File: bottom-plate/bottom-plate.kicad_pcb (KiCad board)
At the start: 2 copper layers, 274.1 x 106.7 mm, 19 parts

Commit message: added logos on silkscreen and plotted all gerber files again
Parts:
- removed the G*** at (158.6, 95.6)
- removed the G*** at (138.5, 95.8)
- removed REF** (x6): Breakaway_Tabs, kbd:Breakaway_Tabs
- removed the Ref** at (248.4, 79.5)
- removed the Ref** at (246.5, 37.4)
- removed the Ref** at (199.2, 80.1)
- removed the Ref** at (269.5, 69.3)
- removed the Ref** at (280.4, 78.5)
- removed the Ref** at (52.0, 85.5)
- removed the Ref** at (98.1, 80.4)
- removed the Ref** at (126.6, 40.9)
- removed the Ref** at (50.7, 37.5)
- removed the Ref** at (27.7, 69.3)
- removed the Ref** at (170.7, 40.9)
- added G***: LOGO, logo:jdkbd-logo1, F.Cu at (47.0, 45.8)
- added G***: LOGO, logo:jdkbd-logo1, B.Cu at (47.0, 45.8)
- added Ref**: Val**, kbd:M2_HOLE_v2, B.Cu at (38.4, 86.7)
- added Ref**: Val**, kbd:M2_HOLE_v2, B.Cu at (148.1, 49.1)
- added Ref**: Val**, kbd:M2_HOLE_v2, B.Cu at (72.2, 45.7)
- added Ref**: Val**, kbd:M2_HOLE_v2, B.Cu at (119.6, 88.4)
- added Ref**: Val**, kbd:M2_HOLE_v2, B.Cu at (70.4, 87.8)
- added Ref**: Val**, kbd:M2_HOLE_v2, B.Cu at (149.4, 86.4)
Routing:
- added copper zone on B.Cu, net (none)
- added copper zone on F.Cu, net (none)
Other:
- board size 274.1 x 106.7 mm -> 134.8 x 106.7 mm
- board text removed: "cornetrack pcb - designed by jannikwibker"
- board text removed: "left pcb"
- board text removed: "right pcb"

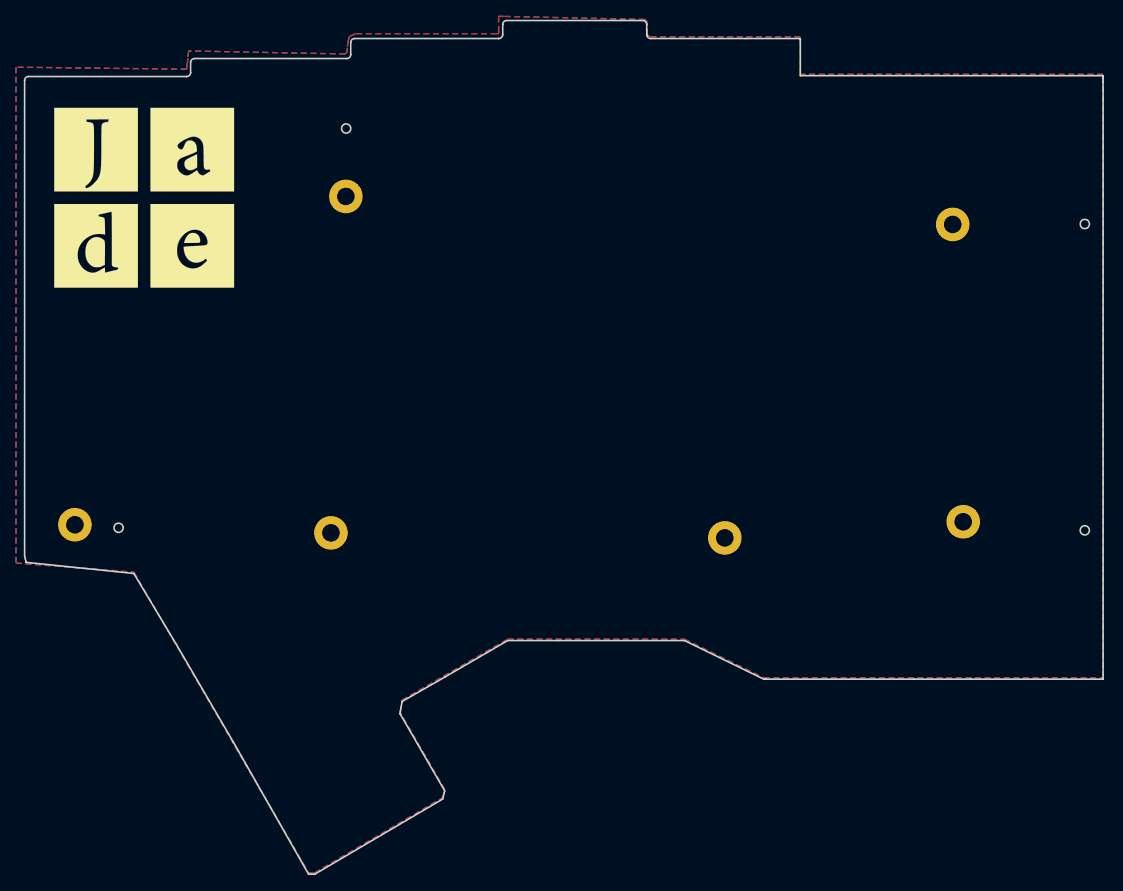
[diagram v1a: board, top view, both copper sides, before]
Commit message: made top and bottom plate a tiny bit larger in order to increase distance between edge cuts to >2mm
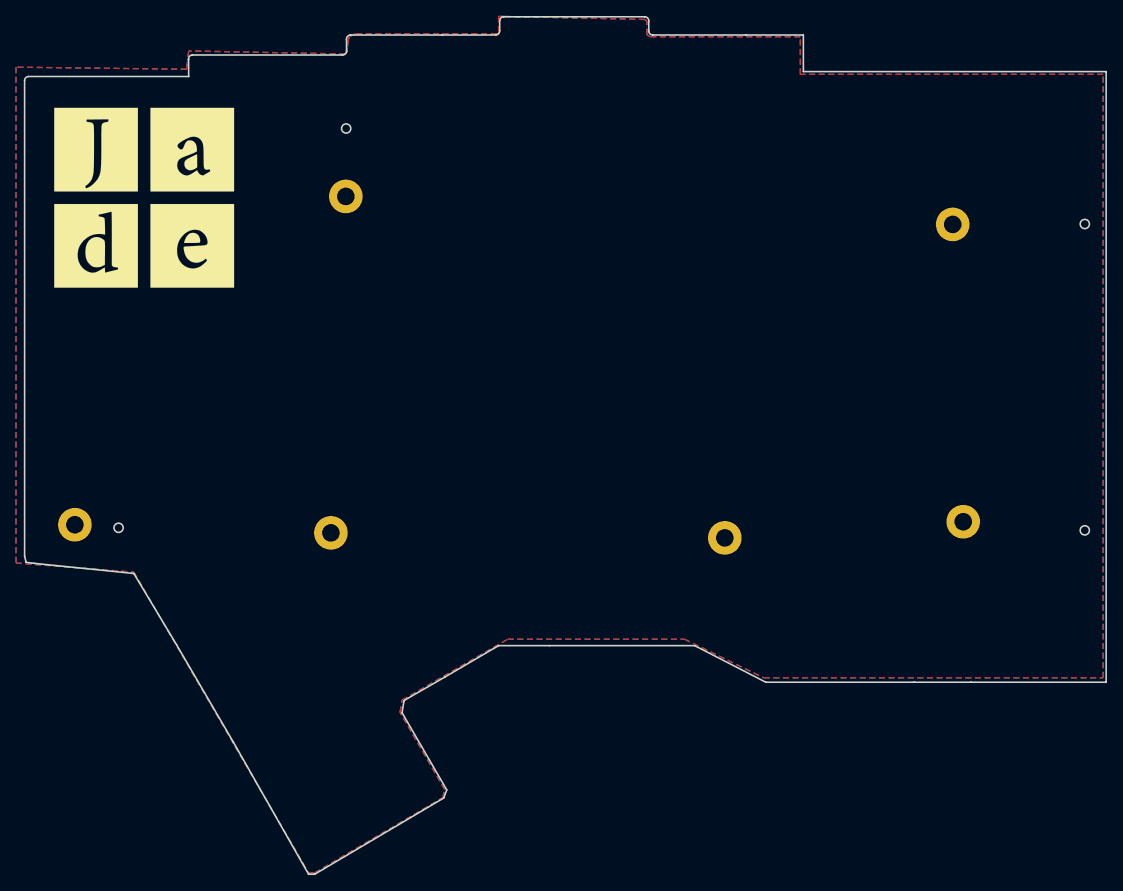
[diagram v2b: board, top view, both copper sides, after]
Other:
- board size 134.8 x 106.7 mm -> 135.2 x 107.2 mm
